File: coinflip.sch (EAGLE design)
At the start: 17 parts, among them IC1 LM358N, IC2 4027N, T1 2N3904, T2 2N3904

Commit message: Version 2.0 commit
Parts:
- added C4: 10uF, rcl:C-US025-024X044
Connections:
- net GND: now also C4.2
- net VDD: now also C4.1
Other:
- note added: "Digital Coin Flip v2"
- note removed: "Digital Coin Flip v1"
- moved on the sheet: IC2A, IC2P, JP1, LED1, LED2, R5, T1, T2

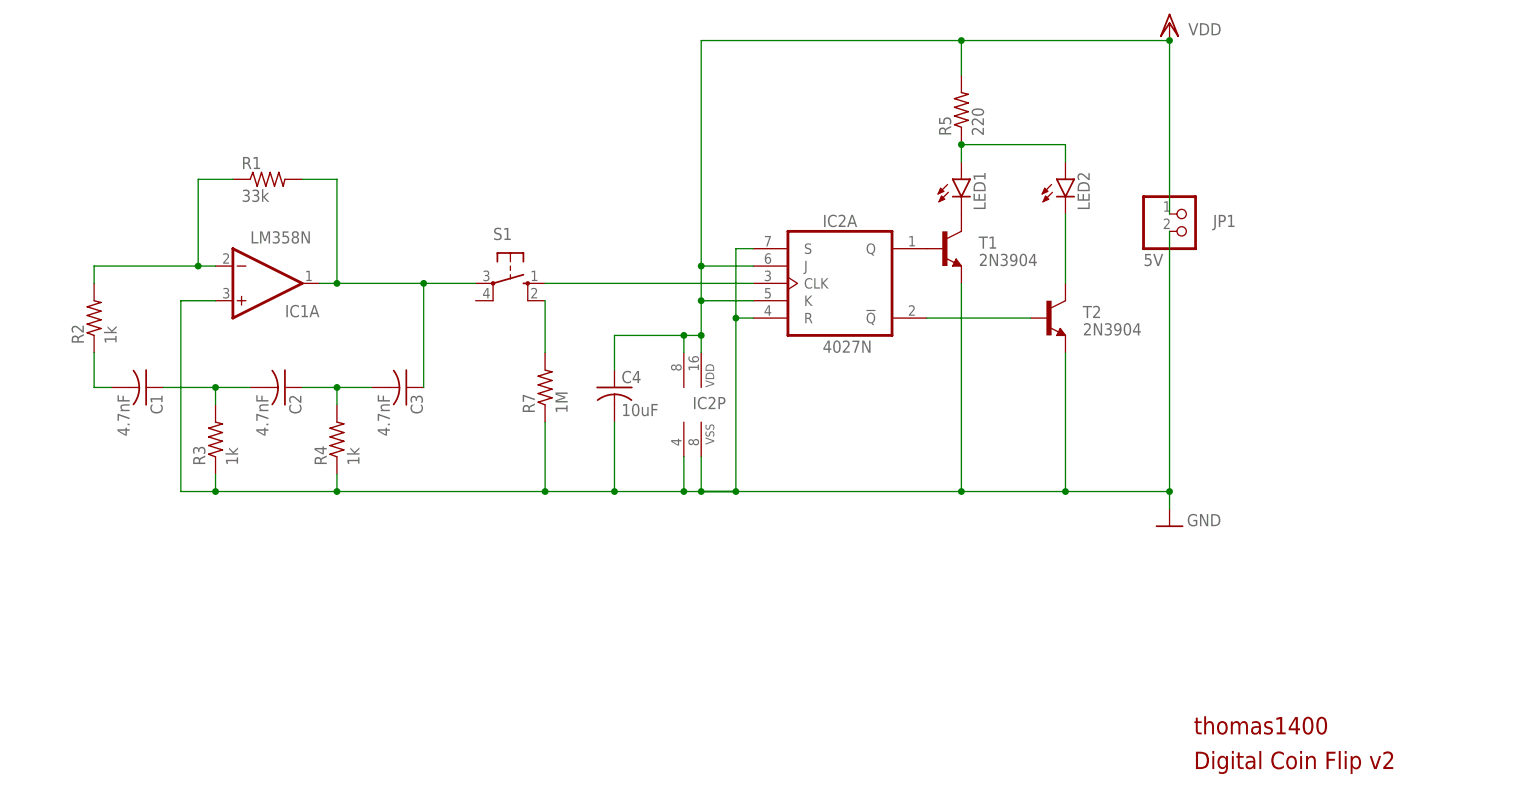
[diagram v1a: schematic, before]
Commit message: Updated to v3.0: redesigned oscillator, new board layout
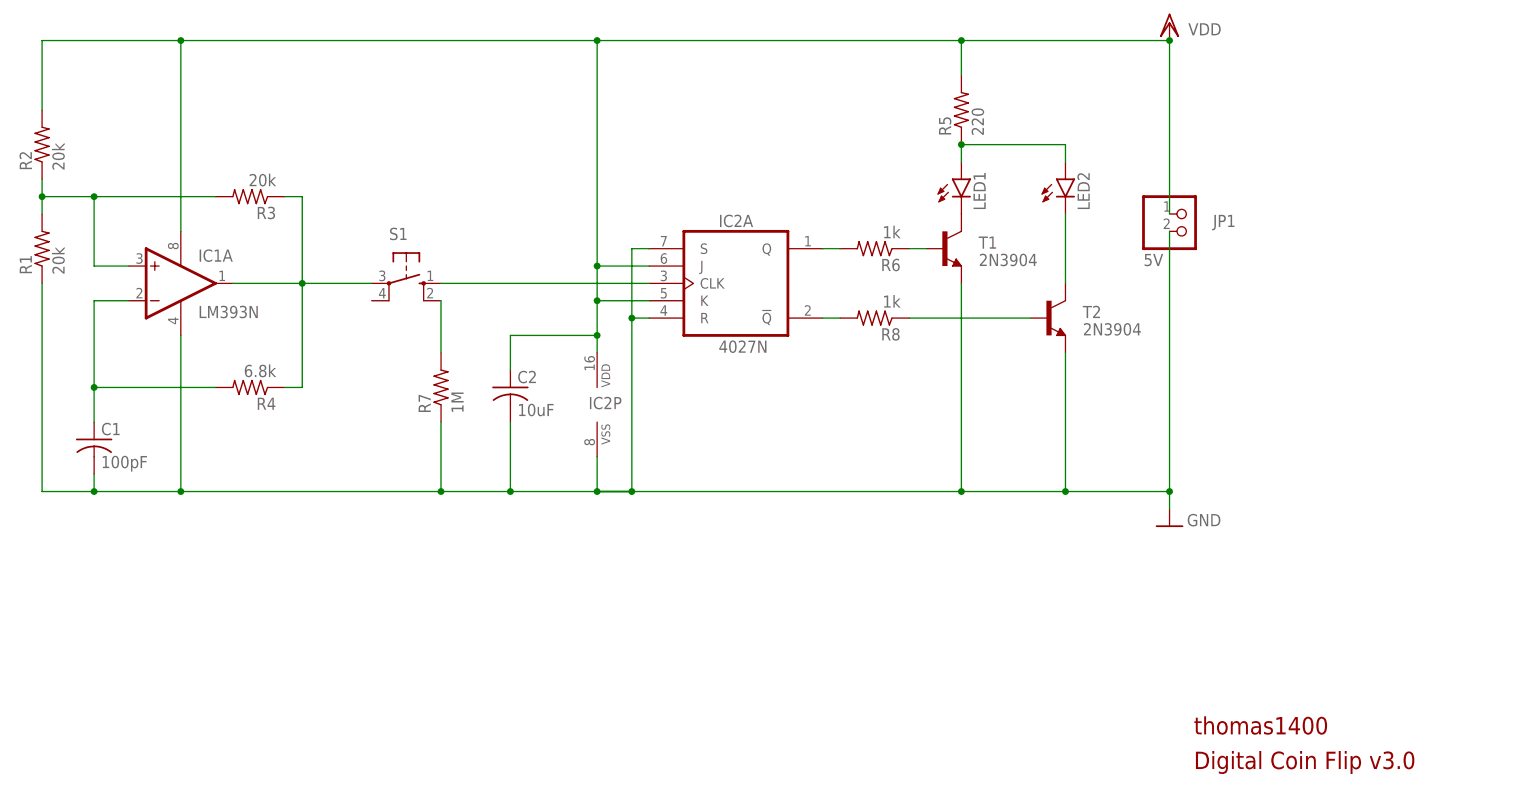
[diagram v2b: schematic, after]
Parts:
- removed C3: 4.7nF, rcl:C-US025-024X044
- removed C4: 10uF, rcl:C-US025-024X044
- added R6, R8: 1k, resistor:R-US_0207/10
- C1: value 4.7nF -> 100pF; device rcl:C-US025-024X044 -> resistor:C-US050-024X044
- C2: value 4.7nF -> 10uF; device rcl:C-US025-024X044 -> resistor:C-US050-024X044
- IC1: value LM358N -> LM393N; device linear:LM358N -> linear:LM393N
- LED1, LED2: device led:LED3MM -> led_nofill:LED3MM
- R1: value 33k -> 20k
- R2, R3: value 1k -> 20k
- R4: value 1k -> 6.8k
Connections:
- removed net N$11: IC2A.!Q, T2.B
- new net N$7: IC2A.!Q, R8.2
- net GND: now also C1.2, C2.2, R1.1; no longer C4.2, IC1A.+IN, R3.1, R4.1
- net N$1: now also IC1A.OUT, R3.1, R4.1, S1.P; no longer C1.2, R2.1
- net N$2: now also IC1A.+IN, R1.2, R2.1; no longer C1.1, C2.2
- net N$3: now also C1.1, IC1A.-IN; no longer C2.1, C3.2
- net N$4: now also IC2A.Q, R6.2; no longer IC1A.-IN, R1.1, R2.2
- net N$6: now also R6.1, T1.B; no longer C3.1, IC1A.OUT, R1.2, S1.P
- net N$8: now also R8.1, T2.B; no longer IC2A.Q, T1.B
- net VDD: now also C2.1, R2.2; no longer C4.1
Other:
- note added: "Digital Coin Flip v3.0"
- note removed: "Digital Coin Flip v2"
- moved on the sheet: C1, C2, IC1A, IC2A, IC2P, R1, R2, R3, R4, R7, S1

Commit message: Version 3.1, added BOM and adjusted routing and silkscreen
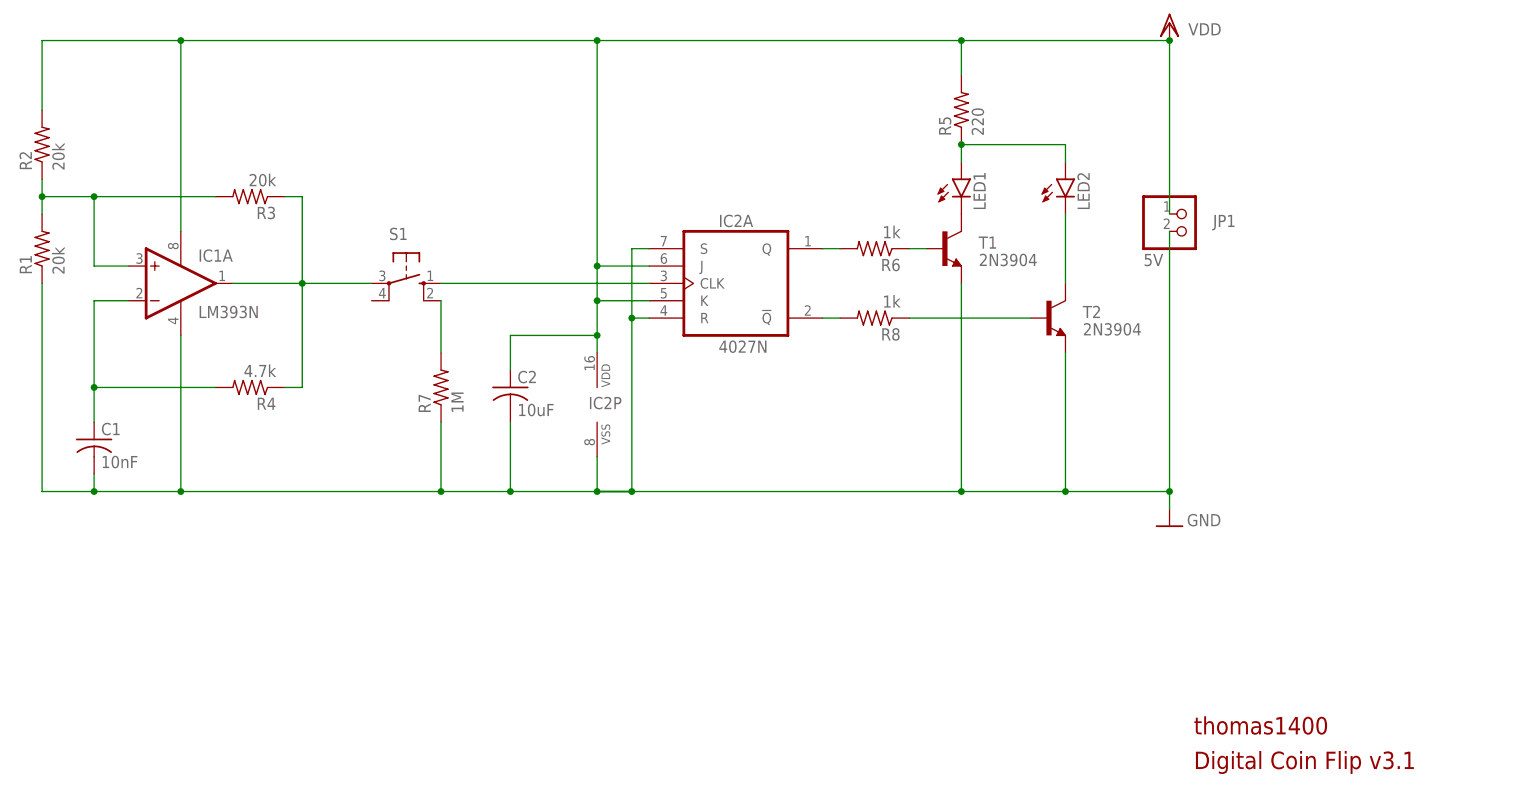
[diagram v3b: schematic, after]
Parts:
- C1: value 100pF -> 10nF; device resistor:C-US050-024X044 -> resistor_nofill:C-US050-024X044
- C2: device resistor:C-US050-024X044 -> resistor_nofill:C-US050-024X044
- R4: value 6.8k -> 4.7k
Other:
- note added: "Digital Coin Flip v3.1"
- note removed: "Digital Coin Flip v3.0"
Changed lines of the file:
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@@
 <grid distance="0.1" unitdist="inch" unit="inch" style="lines" multiple="1" display="no" altdistance="0.01" altunitdist="inch" altunit="inch"/>
 <layers>
-<layer number="1" name="Top" color="4" fill="1" visible="yes" active="no"/>
-<layer number="2" name="Route2" color="16" fill="1" visible="yes" active="no"/>
-<layer number="3" name="Route3" color="17" fill="1" visible="yes" active="no"/>
-<layer number="4" name="Route4" color="18" fill="1" visible="yes" active="no"/>
-<layer number="5" name="Route5" color="19" fill="1" visible="yes" active="no"/>
-<layer number="6" name="Route6" color="25" fill="1" visible="yes" active="no"/>
-<layer number="7" name="Route7" color="26" fill="1" visible="yes" active="no"/>
-<layer number="8" name="Route8" color="27" fill="1" visible="yes" active="no"/>
-<layer number="9" name="Route9" color="28" fill="1" visible="yes" active="no"/>
-<layer number="10" name="Route10" color="29" fill="1" visible="yes" active="no"/>
-<layer number="11" name="Route11" color="30" fill="1" visible="yes" active="no"/>
-<layer number="12" name="Route12" color="20" fill="1" visible="yes" active="no"/>
-<layer number="13" name="Route13" color="21" fill="1" visible="yes" active="no"/>
-<layer number="14" name="Route14" color="22" fill="1" visible="yes" active="no"/>
-<layer number="15" name="Route15" color="23" fill="1" visible="yes" active="no"/>
-<layer number="16" name="Bottom" color="1" fill="1" visible="yes" active="no"/>
-<layer number="17" name="Pads" color="2" fill="1" visible="yes" active="no"/>
-<layer number="18" name="Vias" color="2" fill="1" visible="yes" active="no"/>
-<layer number="19" name="Unrouted" color="6" fill="1" visible="yes" active="no"/>
-<layer number="20" name="Dimension" color="24" fill="1" visible="yes" active="no"/>
-<layer number="21" name="tPlace" color="7" fill="1" visible="yes" active="no"/>
-<layer number="22" name="bPlace" color="7" fill="1" visible="yes" active="no"/>
-<layer number="23" name="tOrigins" color="15" fill="1" visible="yes" active="no"/>
-<layer number="24" name="bOrigins" color="15" fill="1" visible="yes" active="no"/>
-<layer number="25" name="tNames" color="7" fill="1" visible="yes" active="no"/>
-<layer number="26" name="bNames" color="7" fill="1" visible="yes" active="no"/>
-<layer number="27" name="tValues" color="7" fill="1" visible="yes" active="no"/>
-<layer number="28" name="bValues" color="7" fill="1" visible="yes" active="no"/>
+<layer number="1" name="Top" color="4" fill="1" visible="no" active="no"/>
+<layer number="2" name="Route2" color="16" fill="1" visible="no" active="no"/>
+<layer number="3" name="Route3" color="17" fill="1" visible="no" active="no"/>
+<layer number="4" name="Route4" color="18" fill="1" visible="no" active="no"/>
+<layer number="5" name="Route5" color="19" fill="1" visible="no" active="no"/>
+<layer number="6" name="Route6" color="25" fill="1" visible="no" active="no"/>
+<layer number="7" name="Route7" color="26" fill="1" visible="no" active="no"/>
+<layer number="8" name="Route8" color="27" fill="1" visible="no" active="no"/>
+<layer number="9" name="Route9" color="28" fill="1" visible="no" active="no"/>
+<layer number="10" name="Route10" color="29" fill="1" visible="no" active="no"/>
+<layer number="11" name="Route11" color="30" fill="1" visible="no" active="no"/>
+<layer number="12" name="Route12" color="20" fill="1" visible="no" active="no"/>
+<layer number="13" name="Route13" color="21" fill="1" visible="no" active="no"/>
+<layer number="14" name="Route14" color="22" fill="1" visible="no" active="no"/>
+<layer number="15" name="Route15" color="23" fill="1" visible="no" active="no"/>
+<layer number="16" name="Bottom" color="1" fill="1" visible="no" active="no"/>
+<layer number="17" name="Pads" color="2" fill="1" visible="no" active="no"/>
+<layer number="18" name="Vias" color="2" fill="1" visible="no" active="no"/>
+<layer number="19" name="Unrouted" color="6" fill="1" visible="no" active="no"/>
+<layer number="20" name="Dimension" color="24" fill="1" visible="no" active="no"/>
+<layer number="21" name="tPlace" color="7" fill="1" visible="no" active="no"/>
+<layer number="22" name="bPlace" color="7" fill="1" visible="no" active="no"/>
+<layer number="23" name="tOrigins" color="15" fill="1" visible="no" active="no"/>
+<layer number="24" name="bOrigins" color="15" fill="1" visible="no" active="no"/>
+<layer number="25" name="tNames" color="7" fill="1" visible="no" active="no"/>
+<layer number="26" name="bNames" color="7" fill="1" visible="no" active="no"/>
+<layer number="27" name="tValues" color="7" fill="1" visible="no" active="no"/>
+<layer number="28" name="bValues" color="7" fill="1" visible="no" active="no"/>
 <layer number="29" name="tStop" color="7" fill="3" visible="no" active="no"/>
 <layer number="30" name="bStop" color="7" fill="6" visible="no" active="no"/>
@@
 <layer number="35" name="tGlue" color="7" fill="4" visible="no" active="no"/>
 <layer number="36" name="bGlue" color="7" fill="5" visible="no" active="no"/>
-<layer number="37" name="tTest" color="7" fill="1" visible="yes" active="no"/>
-<layer number="38" name="bTest" color="7" fill="1" visible="yes" active="no"/>
+<layer number="37" name="tTest" color="7" fill="1" visible="no" active="no"/>
+<layer number="38" name="bTest" color="7" fill="1" visible="no" active="no"/>
 <layer number="39" name="tKeepout" color="4" fill="11" visible="no" active="no"/>
 <layer number="40" name="bKeepout" color="1" fill="11" visible="no" active="no"/>
@@
 <layer number="44" name="Drills" color="7" fill="1" visible="no" active="no"/>
 <layer number="45" name="Holes" color="7" fill="1" visible="no" active="no"/>
-<layer number="46" name="Milling" color="3" fill="1" visible="yes" active="no"/>
-<layer number="47" name="Measures" color="7" fill="1" visible="yes" active="no"/>
-<layer number="48" name="Document" color="7" fill="1" visible="yes" active="no"/>
-<layer number="49" name="Reference" color="7" fill="1" visible="yes" active="no"/>
-<layer number="51" name="tDocu" color="7" fill="1" visible="yes" active="no"/>
-<layer number="52" name="bDocu" color="7" fill="1" visible="yes" active="no"/>
+<layer number="46" name="Milling" color="3" fill="1" visible="no" active="no"/>
+<layer number="47" name="Measures" color="7" fill="1" visible="no" active="no"/>
+<layer number="48" name="Document" color="7" fill="1" visible="no" active="no"/>
+<layer number="49" name="Reference" color="7" fill="1" visible="no" active="no"/>
+<layer number="51" name="tDocu" color="7" fill="1" visible="no" active="no"/>
+<layer number="52" name="bDocu" color="7" fill="1" visible="no" active="no"/>
 <layer number="88" name="SimResults" color="9" fill="1" visible="yes" active="yes"/>
 <layer number="89" name="SimProbes" color="9" fill="1" visible="yes" active="yes"/>
@@
 <part name="R2" library="resistor" library_urn="urn:adsk.eagle:library:348" deviceset="R-US_" device="0207/10" package3d_urn="urn:adsk.eagle:package:23491/2" value="20k"/>
 <part name="R3" library="resistor" library_urn="urn:adsk.eagle:library:348" deviceset="R-US_" device="0207/10" package3d_urn="urn:adsk.eagle:package:23491/2" value="20k"/>
-<part name="R4" library="resistor" library_urn="urn:adsk.eagle:library:348" deviceset="R-US_" device="0207/10" package3d_urn="urn:adsk.eagle:package:23491/2" value="6.8k"/>
+<part name="R4" library="resistor" library_urn="urn:adsk.eagle:library:348" deviceset="R-US_" device="0207/10" package3d_urn="urn:adsk.eagle:package:23491/2" value="4.7k"/>
 <part name="R5" library="resistor" library_urn="urn:adsk.eagle:library:348" deviceset="R-US_" device="0207/10" package3d_urn="urn:adsk.eagle:package:23491/2" value="220"/>
 <part name="JP1" library="pinhead" library_urn="urn:adsk.eagle:library:325" deviceset="PINHD-1X2" device="" package3d_urn="urn:adsk.eagle:package:22435/2" value="5V"/>
@@
 <part name="FRAME2" library="frames" library_urn="urn:adsk.eagle:library:229" deviceset="A4L-LOC" device=""/>
 <part name="IC1" library="linear" library_urn="urn:adsk.eagle:library:262" deviceset="LM393" device="N" package3d_urn="urn:adsk.eagle:package:16409/2"/>
-<part name="C1" library="resistor" library_urn="urn:adsk.eagle:library:348" deviceset="C-US" device="050-024X044" package3d_urn="urn:adsk.eagle:package:23643/1" value="100pF"/>
+<part name="C1" library="resistor_nofill" deviceset="C-US" device="050-024X044" package3d_urn="urn:adsk.eagle:package:23643/1" value="10nF"/>
 <part name="R6" library="resistor" library_urn="urn:adsk.eagle:library:348" deviceset="R-US_" device="0207/10" package3d_urn="urn:adsk.eagle:package:23491/2" value="1k"/>
 <part name="R8" library="resistor" library_urn="urn:adsk.eagle:library:348" deviceset="R-US_" device="0207/10" package3d_urn="urn:adsk.eagle:package:23491/2" value="1k"/>
-<part name="C2" library="resistor" library_urn="urn:adsk.eagle:library:348" deviceset="C-US" device="050-024X044" package3d_urn="urn:adsk.eagle:package:23643/1" value="10uF"/>
+<part name="C2" library="resistor_nofill" deviceset="C-US" device="050-024X044" package3d_urn="urn:adsk.eagle:package:23643/1" value="10uF"/>
 </parts>
 <sheets>
 <sheet>
 <plain>
-<text x="216.916" y="15.24" size="2.54" layer="94">Digital Coin Flip v3.0</text>
+<text x="216.916" y="15.24" size="2.54" layer="94">Digital Coin Flip v3.1</text>
 <text x="216.916" y="20.32" size="2.54" layer="94">thomas1400</text>
 </plain>
